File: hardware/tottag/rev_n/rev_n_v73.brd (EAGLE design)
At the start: 68.1 x 36.9 mm, 197 parts, among them J1 TC2030-JLINK-NL-2SIDE, J2 TC2030-JLINK-NL-2SIDE, J4 MOLEX-PICO-SPOX-3SIDE, Q1 CSD75207W15, Q2 MOSFET-NCHANNELXFDN-3, U1 APOLLO4_BLUE_PLUS_SOC_KBR, U2 DW3110, U3 BQ24040, U4 BQ51013B, U6 BNO086, U7 QM14068, U8 AS5FXXX04SND, X1 ABM12W, X2 TXC-9HT12, X3 TXC-9HT12

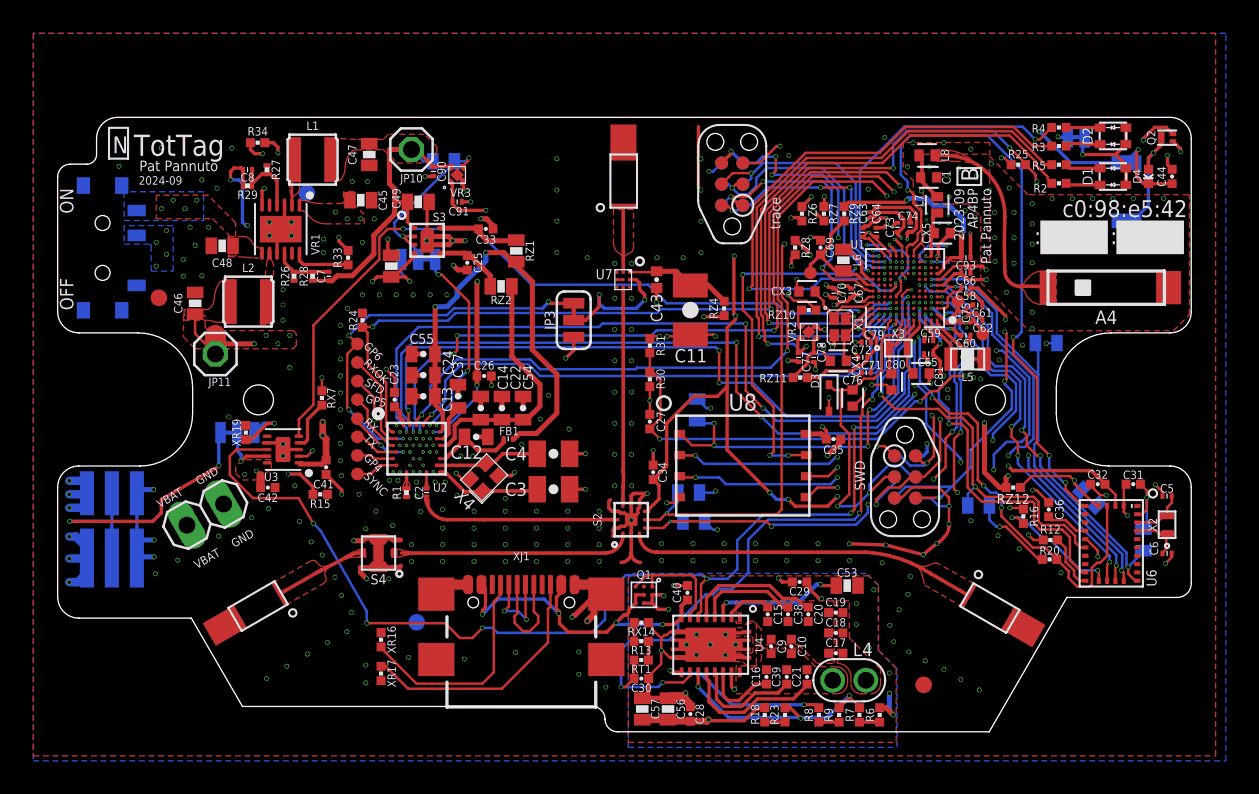
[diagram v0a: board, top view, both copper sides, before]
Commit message: rev_n: manufacturing fixes
 - Fix U2 footprint
 - Add tCream for S4
 - Fix AP4/9DOF SPI/I2C mux mismatch with SJ's
    - Removes RX9 and RZ12
 - Rename solder jumpers as SJ#
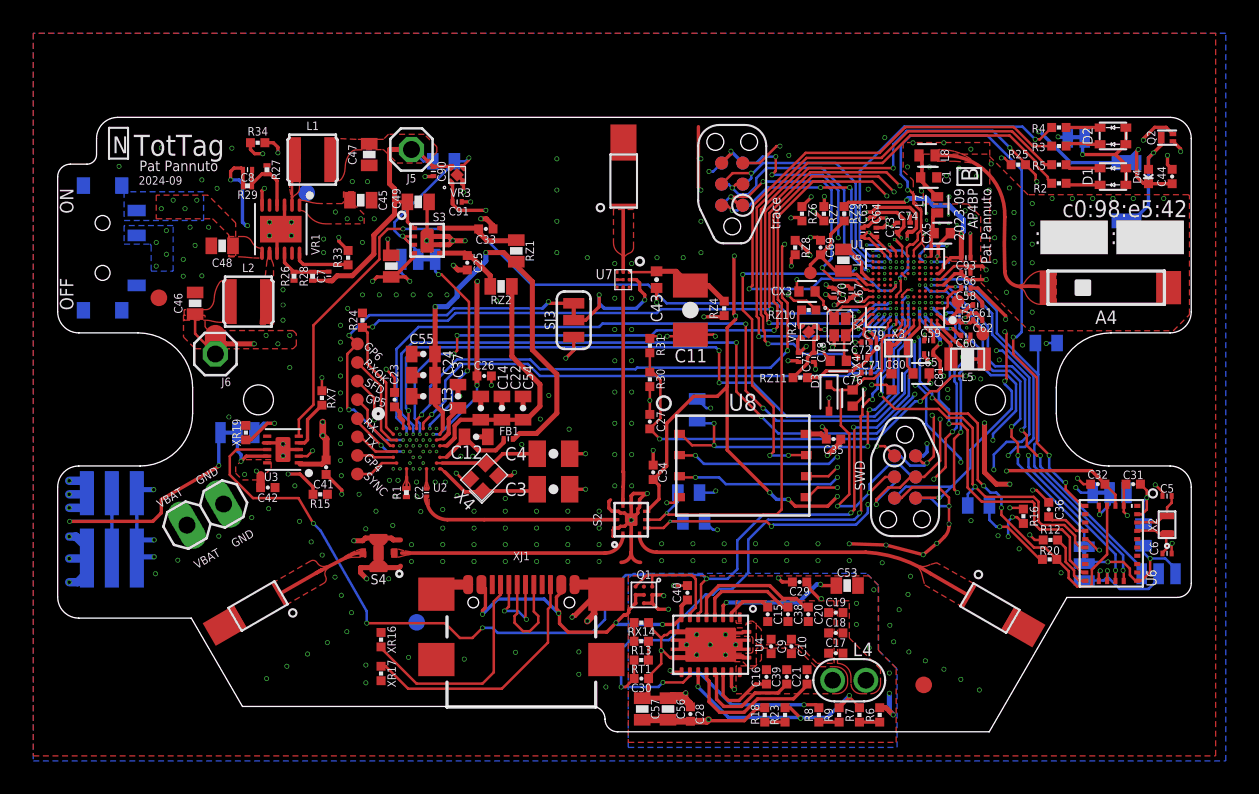
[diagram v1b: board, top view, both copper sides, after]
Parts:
- removed RX9: DNP, passives:0603-RES
- removed RZ12: 0, passives:0402_RES
- added SJ5, SJ6, SJ7: JUMPER-SMT_3_1-NC_TRACE_SILK, SparkFun-Jumpers:SMT-JUMPER_3_1-NC_TRACE_SILK
- moved RX5 0.30 mm to (31.2, 5.38)
- renumbered JP1 to SJ1, JP10 to J5, JP11 to J6, JP12 to SJ4, JP2 to SJ2, JP3 to SJ3, JP9 to J3
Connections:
- removed net AP4_GP09/TT_9DOF_H_SDA/H_MISO/TX: RX5.2, U1.G2, U6.20
- removed net AP4_GP10/TT_9DOF_SA0/H_MOSI: U1.G3, U6.17
- new net 9DOF_H_SDA/H_MISO/TX: RX5.2, SJ5.1, SJ6.2, U6.20
- new net 9DOF_SA0/H_MOSI: SJ5.2, SJ6.1, U6.17
- new net AP4_GP09/TT_9DOF_H_MOSI: SJ5.3, U1.G2
- new net AP4_GP10/TT_9DOF_H_MISO: SJ6.3, U1.G3
- net +1V8: now also SJ7.3; no longer RZ12.2
- net BNO_PS1: now also SJ7.2; no longer RX9.2, RZ12.1
- net GND: now also SJ7.1; no longer RX9.1
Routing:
- net AP4_GP09/TT_9DOF_H_SDA/H_MISO/TX: track 25.7 -> 0.00 mm, vias 4 -> 0
- net AP4_GP10/TT_9DOF_SA0/H_MOSI: track 24.1 -> 0.00 mm, vias 4 -> 0
- net AP4_GP09/TT_9DOF_H_MOSI: track 0.00 -> 24.0 mm, vias 0 -> 3
- net AP4_GP10/TT_9DOF_H_MISO: track 0.00 -> 21.3 mm, vias 0 -> 3
- net 9DOF_H_SDA/H_MISO/TX: track 0.00 -> 8.77 mm, vias 0 -> 2
- net 9DOF_SA0/H_MOSI: track 0.00 -> 6.40 mm, vias 0 -> 1
- net BNO_PS1: track 6.60 -> 2.12 mm
- net GND: track 223.7 -> 222.4 mm
- net BNO_ENV_SDA: track 7.97 -> 9.13 mm, vias 2 -> 3
- net +1V8: track 215.5 -> 214.7 mm, vias 34 -> 35
